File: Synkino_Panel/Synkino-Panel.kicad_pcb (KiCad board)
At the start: 2 copper layers, 93.3 x 69.3 mm, 8 parts, among them SW1 Power, SW2 Rotary_Encoder_Switch, SW3 Reset, U4 SPIOLED128x64

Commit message: Pre Footprint-Fixing State
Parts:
- removed SW1: Power, easyEDA:KEY-SMD_4P-L12.0-W12.0-P5.00-LS15.2
- removed SW2: Rotary_Encoder_Switch, Peacemans_Footprints:SW_PEC11
- removed SW3: Reset, easyEDA:KEY-SMD_4P-L6.0-W6.0-P4.50-LS8.6
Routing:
- net (no net): track 0.75 -> 0.00 mm
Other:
- outline, holes or cut-outs redrawn

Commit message: Rev.G as ordered, inclduing new panel
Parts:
- removed U4: SPIOLED128x64, Peacemans_Footprints:SPIOLED
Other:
- outline, holes or cut-outs redrawn
- board text added: "Synkino"
- board text added: "by filmkorn.org"

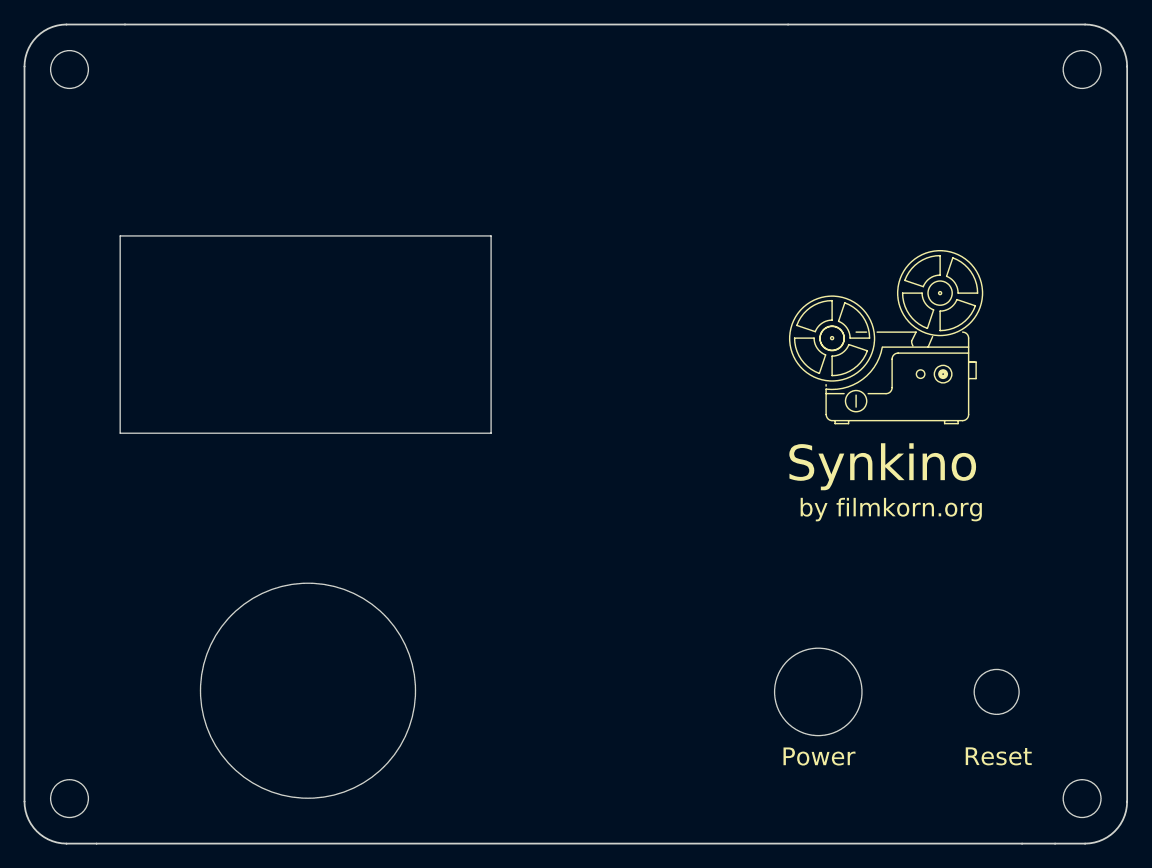
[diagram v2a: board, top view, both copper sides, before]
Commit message: Put Impulse LED behind Logo's Lens, move Display Cutout 0.9mm lower and 0.5,, to the left, make Projector artwork partially translucent, get HASL on the artwork reels, make Power Button Hole have 1mm less diameter
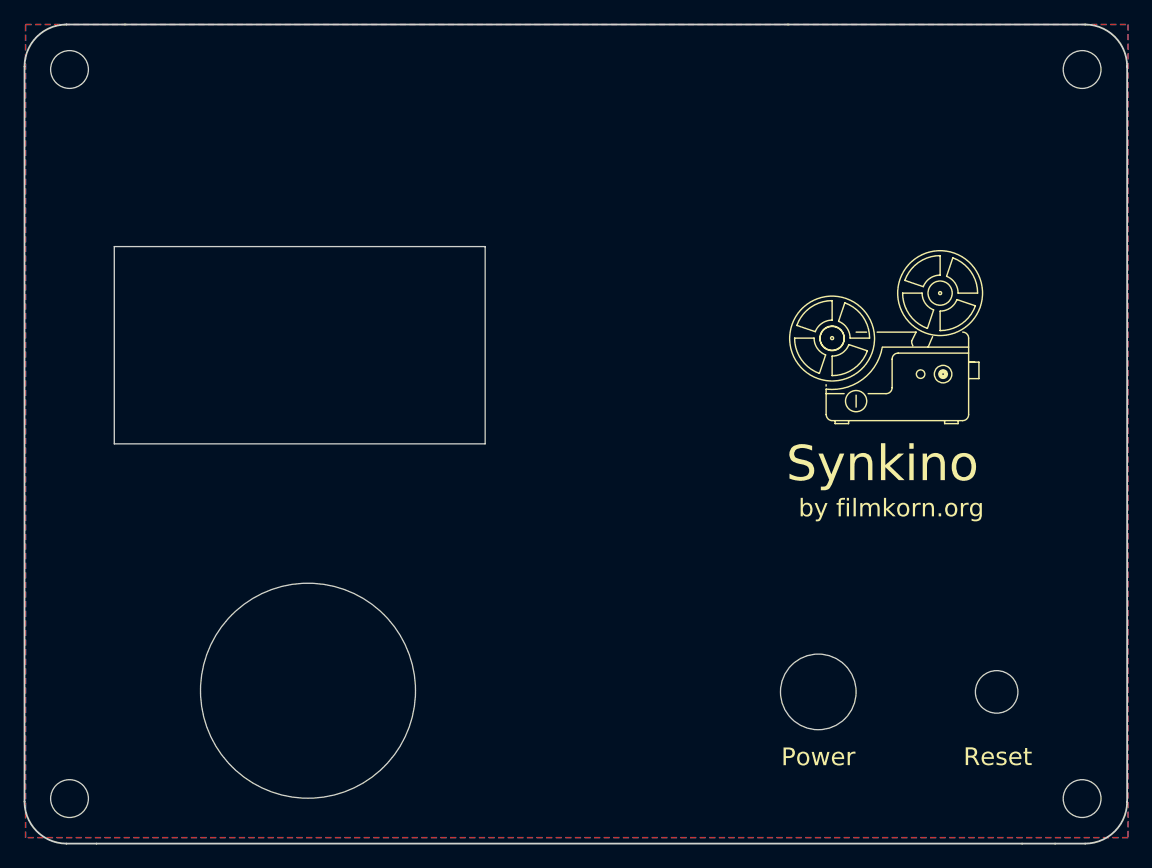
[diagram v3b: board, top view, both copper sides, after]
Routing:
- added copper zone on B.Cu, net (none)
- added copper zone on F.Cu, net (none)
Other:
- outline, holes or cut-outs redrawn

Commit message: Panel Rev.B as ordered
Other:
- board text added: "Rev.B"
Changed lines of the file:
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@@
 		(layer "Edge.Cuts")
 	)
-	(gr_text "JLCJLCJLCJLC"
-		(at 134.9 99.6 0)
+	(gr_text "Rev.B"
+		(at 137.6 99.3 0)
 		(layer "B.SilkS")
 		(effects
+			(font
+				(size 1 1)
+				(thickness 0.1)
+			)
+			(justify left bottom mirror)
+		)
+	)
+	(gr_text "JLCJLCJLCJLC"
+		(at 131.8 99.3 0)
+		(layer "B.SilkS")
+		(effects

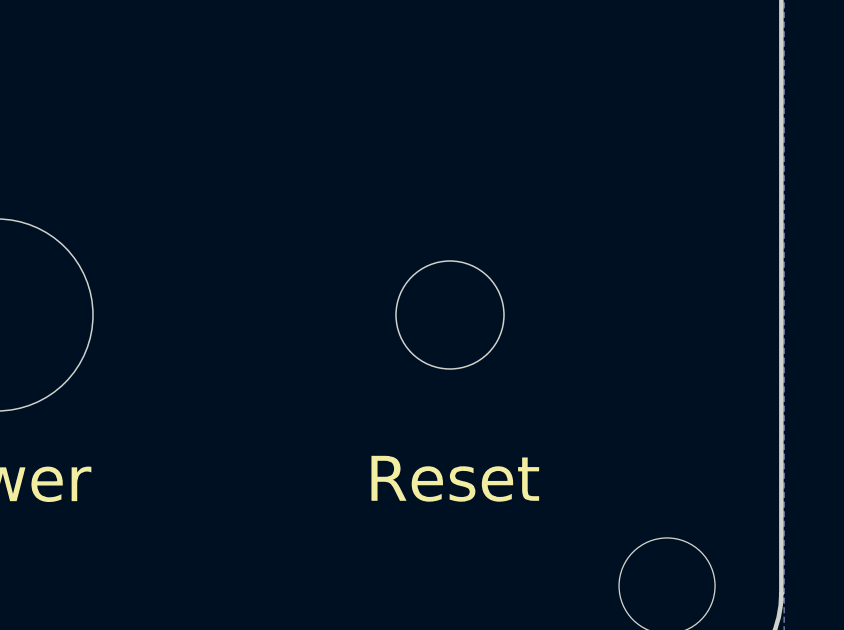
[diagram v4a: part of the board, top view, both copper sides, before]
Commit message: Updating panel to let Projector no longer be translucent
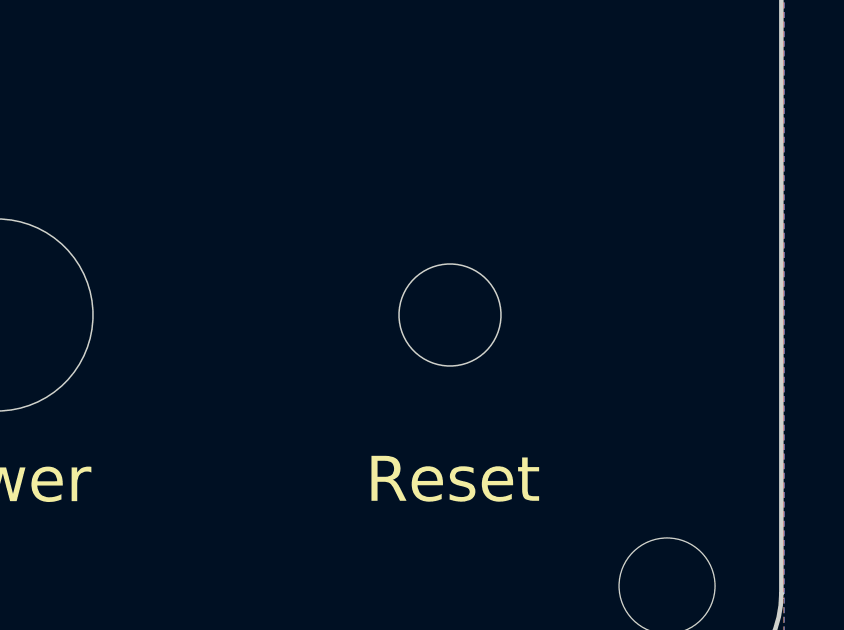
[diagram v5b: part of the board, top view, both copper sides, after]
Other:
- outline, holes or cut-outs redrawn
- board text added: "Rev.C"
- board text removed: "Rev.B"
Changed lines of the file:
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@@
 	(gr_circle
 		(center 188.2 114.1)
-		(end 190 114.1)
+		(end 189.9 114.1)
 		(stroke
 			(width 0.05)
@@
 		(layer "Edge.Cuts")
 	)
-	(gr_text "Rev.B"
+	(gr_text "Rev.C"
 		(at 137.6 99.3 0)
 		(layer "B.SilkS")
@@
 			)
 		)
-	)
-	(zone
-		(net 0)
-		(net_name "")
-		(layer "B.Cu")
-		(hatch edge 0.508)
-		(connect_pads
-			(clearance 0)
-		)
-		(min_thickness 0.254)
-		(filled_areas_thickness no)
-		(keepout
-			(tracks not_allowed)
-			(vias not_allowed)
-			(pads allowed)
-			(copperpour not_allowed)
-			(footprints allowed)
-		)
-		(fill
-			(thermal_gap 0.508)
-			(thermal_bridge_width 0.508)
-		)
-		(polygon
-			(pts
-				(xy 182.65079 83.89579) (xy 183.79379 83.89579) (xy 184.42879 83.76879) (xy 184.93679 83.64179)
-				(xy 185.31779 83.64179) (xy 185.57179 83.76879) (xy 185.82579 84.02279) (xy 185.82579 86.18179)
-				(xy 185.82579 87.57879) (xy 185.82579 90.75379) (xy 185.69879 91.00779) (xy 185.31779 91.13479)
-				(xy 184.93679 91.13479) (xy 184.93679 91.38879) (xy 183.79379 91.38879) (xy 183.79379 91.13479)
-				(xy 175.79279 91.13479) (xy 175.79279 91.38879) (xy 174.64979 91.38879) (xy 174.64979 91.13479)
-				(xy 174.14179 91.13479) (xy 173.88779 91.00779) (xy 173.76079 90.75379) (xy 173.76079 87.83279)
-				(xy 174.64979 87.83279) (xy 175.28479 87.70579) (xy 176.04679 87.32479) (xy 176.80879 86.81679)
-				(xy 177.18979 86.30879) (xy 177.57079 85.67379) (xy 177.82479 84.91179) (xy 177.95179 84.14979)
-				(xy 177.95179 83.64179) (xy 182.01579 83.64179)
-			)
-		)
